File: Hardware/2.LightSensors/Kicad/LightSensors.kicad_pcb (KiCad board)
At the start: 2 copper layers, 0 parts

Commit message: Add update PCB dimension
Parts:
- added C1: 100nF, Capacitor_SMD:C_0402_1005Metric, F.Cu at (90.7, 86.9)
- added C2: 100nF, Capacitor_SMD:C_0402_1005Metric, F.Cu at (90.7, 88.8)
- added C3: 100nF, Capacitor_SMD:C_0402_1005Metric, F.Cu at (90.7, 90.8)
- added C4: 100nF, Capacitor_SMD:C_0402_1005Metric, F.Cu at (130.8, 110.5)
- added H1: MountingHole, MountingHole:MountingHole_3.2mm_M3_ISO7380, F.Cu at (81.3, 81.3)
- added H2: MountingHole, MountingHole:MountingHole_3.2mm_M3_ISO7380, F.Cu at (81.3, 121.9)
- added H3: MountingHole, MountingHole:MountingHole_3.2mm_M3_ISO7380, F.Cu at (172.7, 81.3)
- added H4: MountingHole, MountingHole:MountingHole_3.2mm_M3_ISO7380, F.Cu at (172.7, 122.2)
- added J1: Conn_01x10_Pin, Connector_JST:JST_PH_S10B-PH-K_1x10_P2.00mm_Horizontal, F.Cu at (147.6, 110.2)
- added JP1: SolderJumper_3_Open, Jumper:SolderJumper-3_P2.0mm_Open_TrianglePad1.0x1.5mm, F.Cu at (83.3, 102.1)
- added JP2: SolderJumper_3_Open, Jumper:SolderJumper-3_P2.0mm_Open_TrianglePad1.0x1.5mm, F.Cu at (86.4, 102.1)
- added JP3: SolderJumper_3_Open, Jumper:SolderJumper-3_P2.0mm_Open_TrianglePad1.0x1.5mm, F.Cu at (135.8, 113.1)
- added R1: 0, NetTie:NetTie-2_THT_Pad0.3mm, F.Cu at (84.1, 89.8)
- added R2: 0, NetTie:NetTie-2_THT_Pad0.3mm, F.Cu at (84.1, 91.4)
- added R3: 3.3M, Capacitor_SMD:C_0402_1005Metric, F.Cu at (90.7, 94.7)
- added R4: 10K, Resistor_SMD:R_0402_1005Metric, F.Cu at (143.3, 91.7)
- added R5: 10k, Resistor_SMD:R_0402_1005Metric, F.Cu at (143.3, 96.3)
- added R6: 10K, Capacitor_SMD:C_0402_1005Metric, F.Cu at (130.8, 114.4)
- added U1: AS7331, AS7331:OLGA-16, F.Cu at (104.6, 102.4)
- added U2: OPT3004, OPT3004:SON65P200X200X65-7N, F.Cu at (134.9, 121.8)
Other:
- board outline added: 101.6 x 50.8 mm

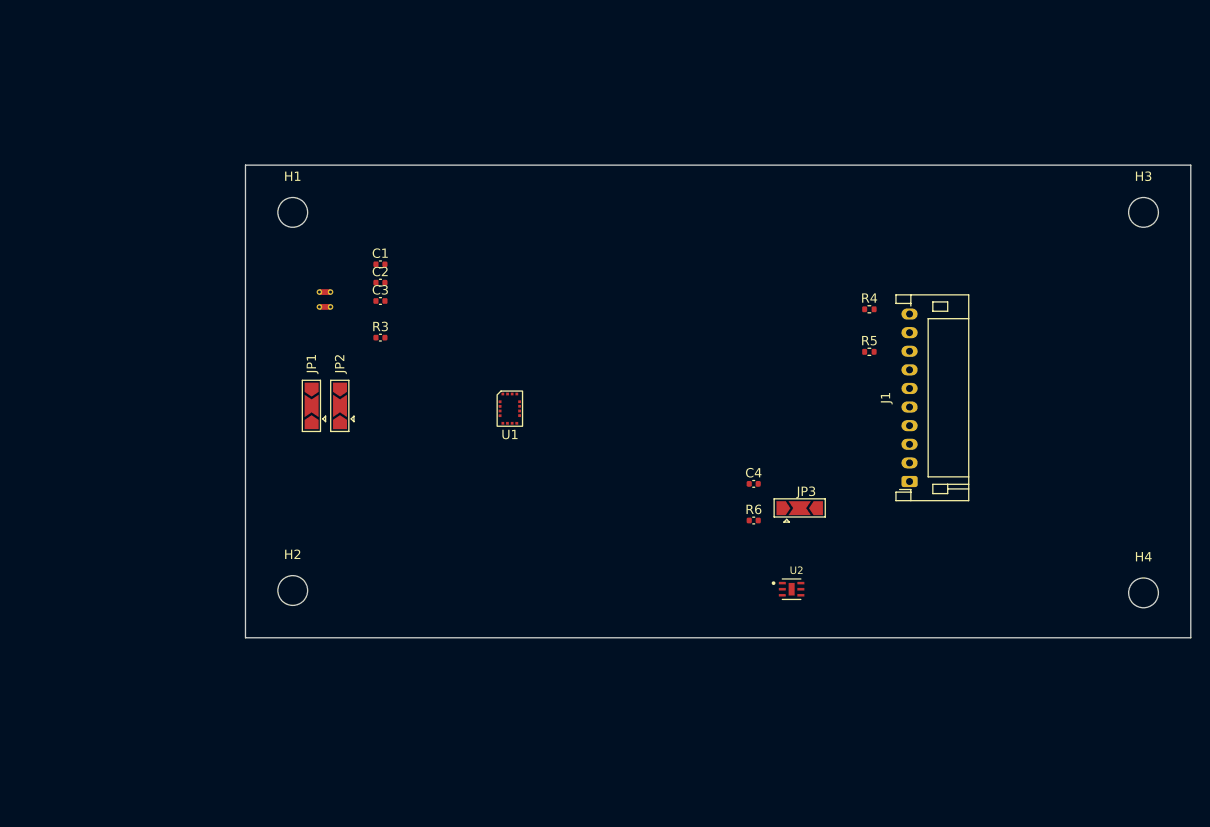
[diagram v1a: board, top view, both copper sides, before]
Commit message: Update PCB for LightSensors
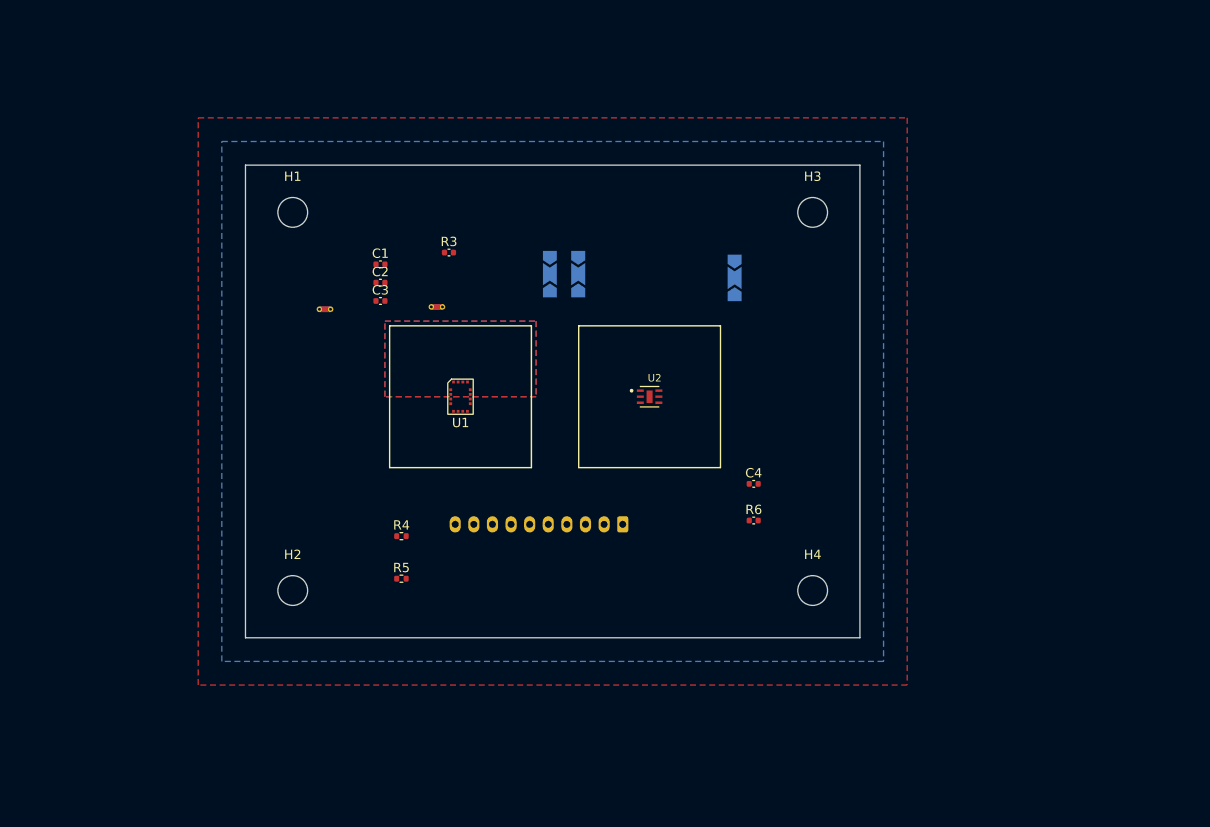
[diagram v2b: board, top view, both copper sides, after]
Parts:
- J1, JP1, JP2, JP3, R1, R2: moved to B.Cu
- moved R4 55.9 mm to (93.0, 116.1)
- moved R5 55.9 mm to (93.0, 120.7)
- moved H4 35.6 mm to (137.2, 121.9)
- moved H3 35.6 mm to (137.2, 81.3)
- moved JP1 32.0 mm to (112.0, 87.9)
- moved J1 31.2 mm to (116.7, 114.8), turned to 180 degrees
- moved JP2 26.6 mm to (108.9, 87.9)
- moved JP3 25.7 mm to (128.8, 88.3), turned to 90 degrees
- moved U2 25.7 mm to (119.6, 101.1)
- moved R2 13.2 mm to (97.4, 91.4), turned to 180 degrees
- moved R3 11.7 mm to (98.1, 85.6)
- moved U1 5.46 mm to (99.3, 101.1)
- moved R1 1.85 mm to (84.1, 91.7)
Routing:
- added copper zone on B.Cu, net +3.3V
- added copper zone on B.Cu, net +3.3VA
- added copper zone on F.Cu, net GND
- added copper zone on F.Cu, net GNDA
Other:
- board size 101.6 x 50.8 mm -> 66 x 50.8 mm

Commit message: Design initial version of PCB for light sensors
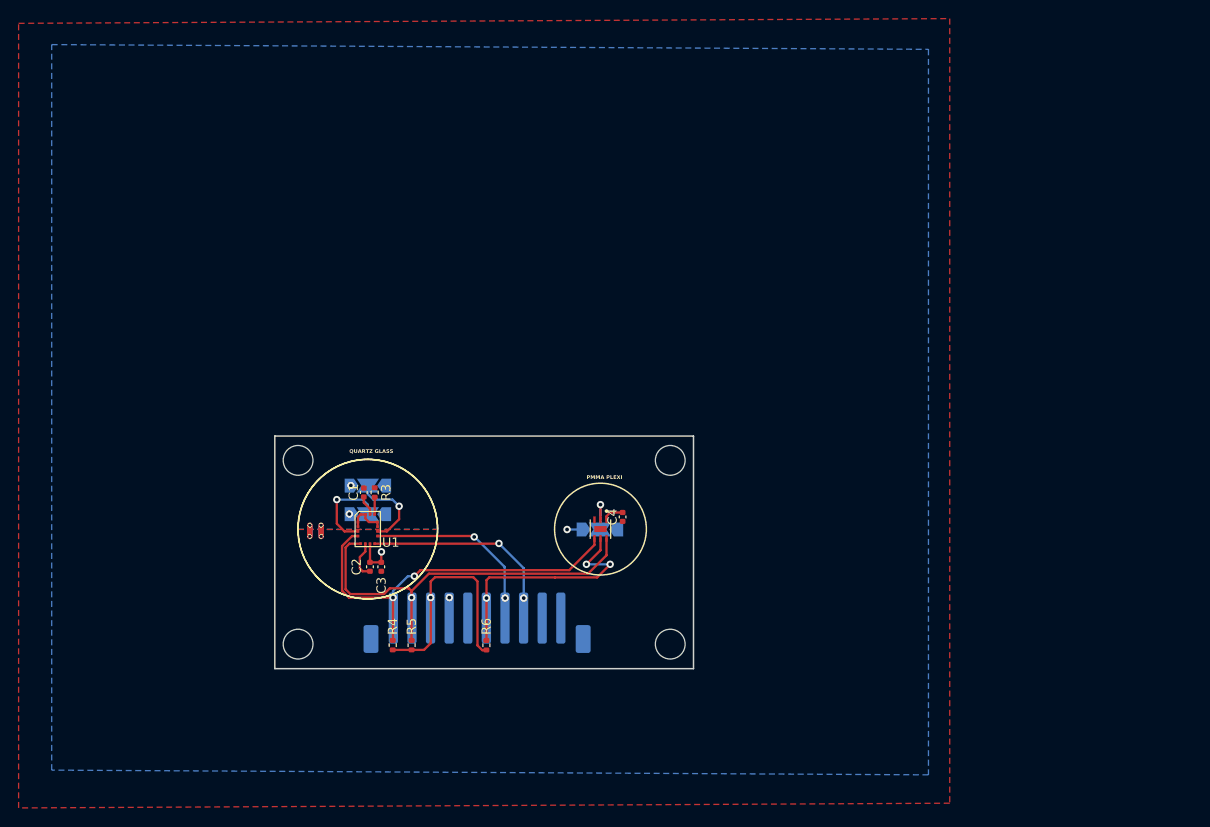
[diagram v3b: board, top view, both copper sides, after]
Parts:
- H1, H2, H3, H4: footprint MountingHole:MountingHole_3.2mm_M3_ISO7380 -> MountingHole:MountingHole_3.2mm_M3
- J1: footprint Connector_JST:JST_PH_S10B-PH-K_1x10_P2.00mm_Horizontal -> Connector_JST:JST_PH_B10B-PH-SM4-TB_1x10-1MP_P2.00mm_Vertical
- R2: moved to F.Cu
- R3, R6: footprint Capacitor_SMD:C_0402_1005Metric -> Resistor_SMD:R_0402_1005Metric
- moved H4 55.6 mm to (81.9, 127.7)
- moved H3 48.9 mm to (121.9, 127.7)
- moved H2 42.9 mm to (121.9, 107.9)
- moved A0 34.3 mm to (89.4, 113.7), turned to 0 degrees
- moved R6 31.7 mm to (102.1, 127.8), turned to 90 degrees
- moved ADDR 30.7 mm to (114.3, 115.4), turned to 0 degrees
- moved C2 30.6 mm to (89.6, 119.4), turned to -90 degrees
- moved A1 30.0 mm to (89.4, 110.6), turned to 0 degrees
- moved C3 28.6 mm to (90.8, 119.4), turned to -90 degrees
- moved R2 28.5 mm to (83.1, 116.1), turned to 90 degrees
- moved R3 27.0 mm to (90.1, 111.4), turned to 90 degrees
- moved H1 26.7 mm to (81.9, 107.9)
- moved C1 24.6 mm to (88.9, 111.4), turned to 90 degrees
- moved R1 24.4 mm to (84.3, 116.1), turned to 90 degrees
- moved J1 18.9 mm to (101.1, 125.4), turned to 0 degrees
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- renumbered JP1 to A0, JP2 to A1, JP3 to ADDR
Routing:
- net I2C_SDA: track 0.00 -> 43.6 mm, vias 0 -> 1
- net I2C_SCL: track 0.00 -> 42.5 mm, vias 0 -> 2
- net +3.3V: track 0.00 -> 33.3 mm, vias 0 -> 2
- net OPT3004_INT: track 0.00 -> 26.5 mm, vias 0 -> 3
- net AS7331_READY: track 0.00 -> 22.5 mm, vias 0 -> 2
- net AS7331_SYN: track 0.00 -> 20.5 mm, vias 0 -> 2
- net ADDR0: track 0.00 -> 9.78 mm, vias 0 -> 1
- net ADDR1: track 0.00 -> 9.08 mm, vias 0 -> 1
- net GND: track 0.00 -> 5.65 mm, vias 0 -> 2
- net GNDA: track 0.00 -> 4.36 mm, vias 0 -> 2
- net Net-(JP3-C): track 0.00 -> 4.24 mm, vias 0 -> 1
- net +3.3VA: track 0.00 -> 2.15 mm
- net Net-(U1-REXT): track 0.00 -> 1.85 mm
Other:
- board size 66 x 50.8 mm -> 45 x 25 mm
- board text added: "1"
- board text added: "1 0"
- board text added: "Address |A1 |A0 0x74 |0 |0 0x75 |0 |1 0x76 |1 |0 0x77 |1 |1"
- board text added: "Address |ADDR 0x44 |0 0x45 |1"
- board text added: "PMMA PLEXI"
- board text added: "QUARTZ GLASS"

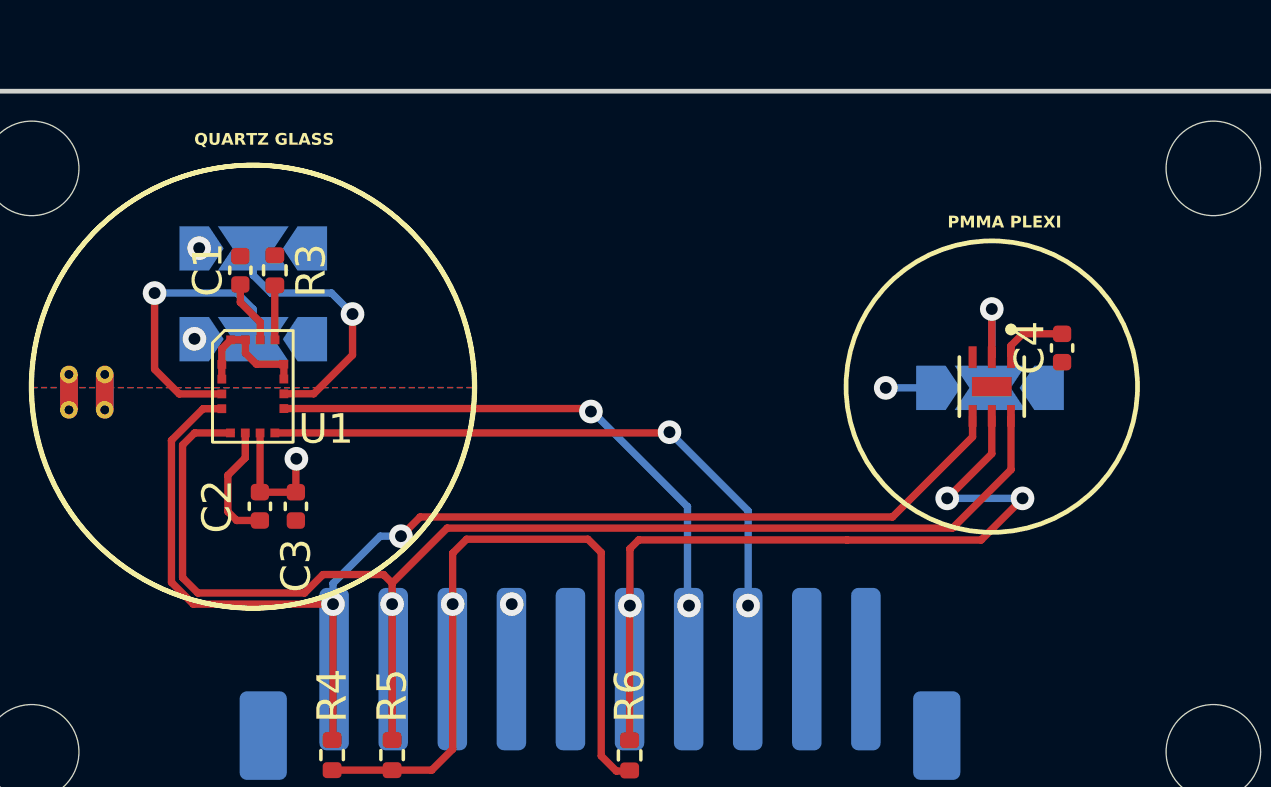
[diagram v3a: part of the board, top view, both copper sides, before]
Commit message: Add signal names on silkscreen and add connector 3dmodel
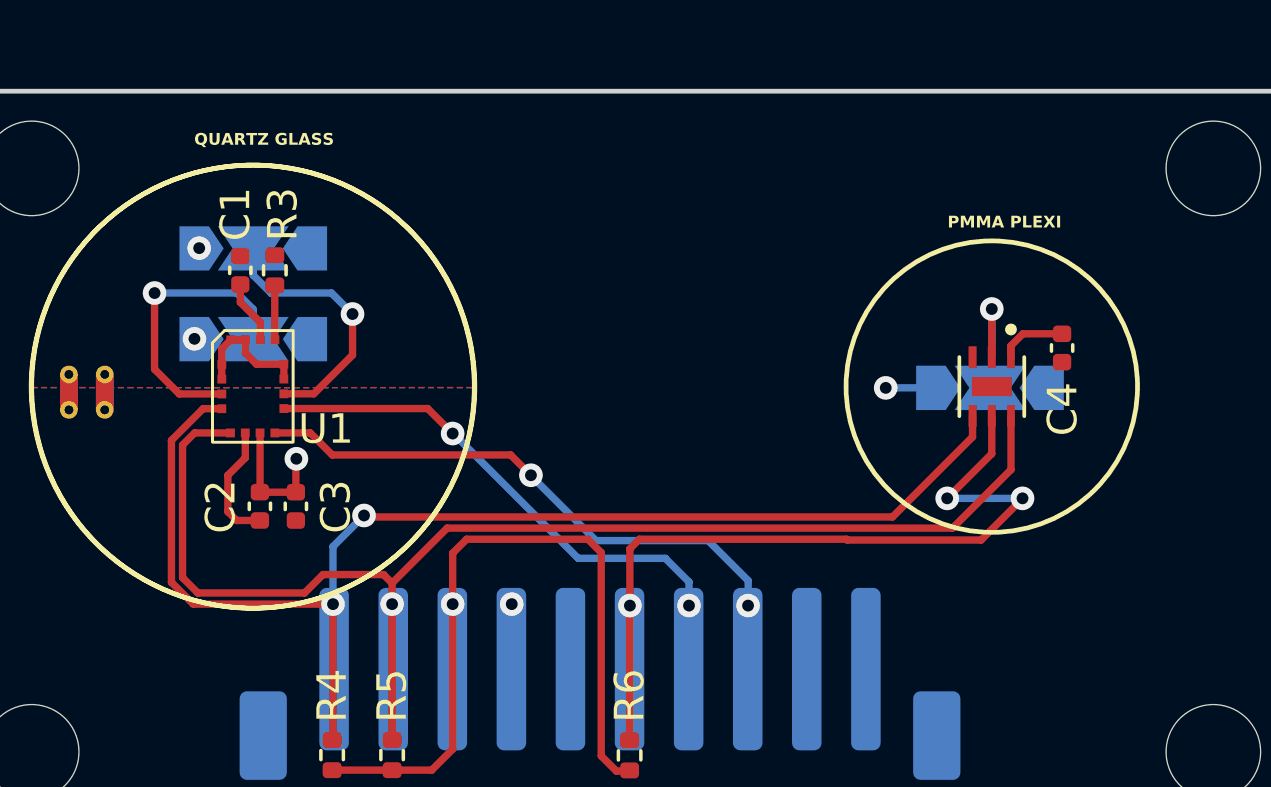
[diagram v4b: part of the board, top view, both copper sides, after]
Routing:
- net AS7331_SYN: track 20.5 -> 19.1 mm
- net AS7331_READY: track 22.5 -> 21.1 mm
- net I2C_SCL: track 42.5 -> 43.2 mm
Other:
- board text added: "3V3"
- board text added: "AS7331_READY"
- board text added: "AS7331_SYN"
- board text added: "GND"
- board text added: "I2C_SCL"
- board text added: "OPT3004_INT"
- board text added: "SCL"
- board text added: "SDA"

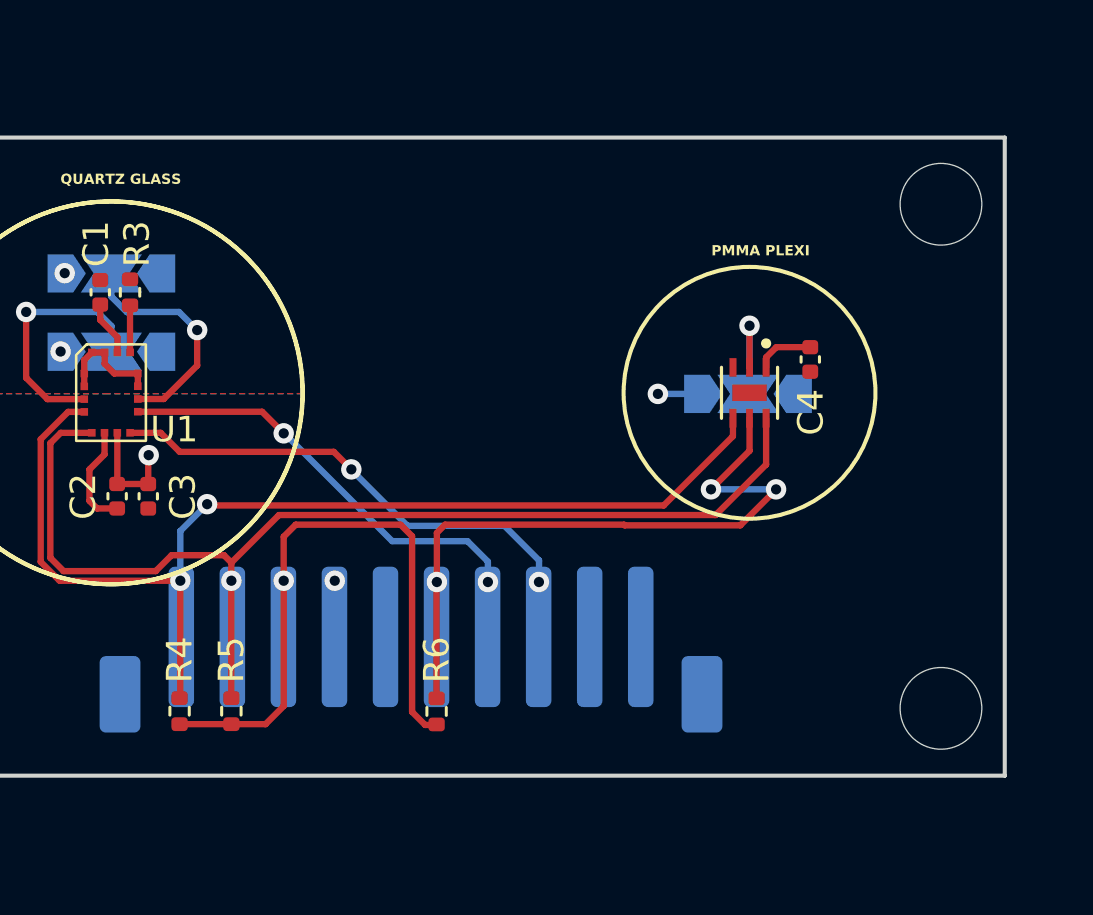
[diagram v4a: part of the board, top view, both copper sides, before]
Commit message: Update pcb due to connector pinout fix
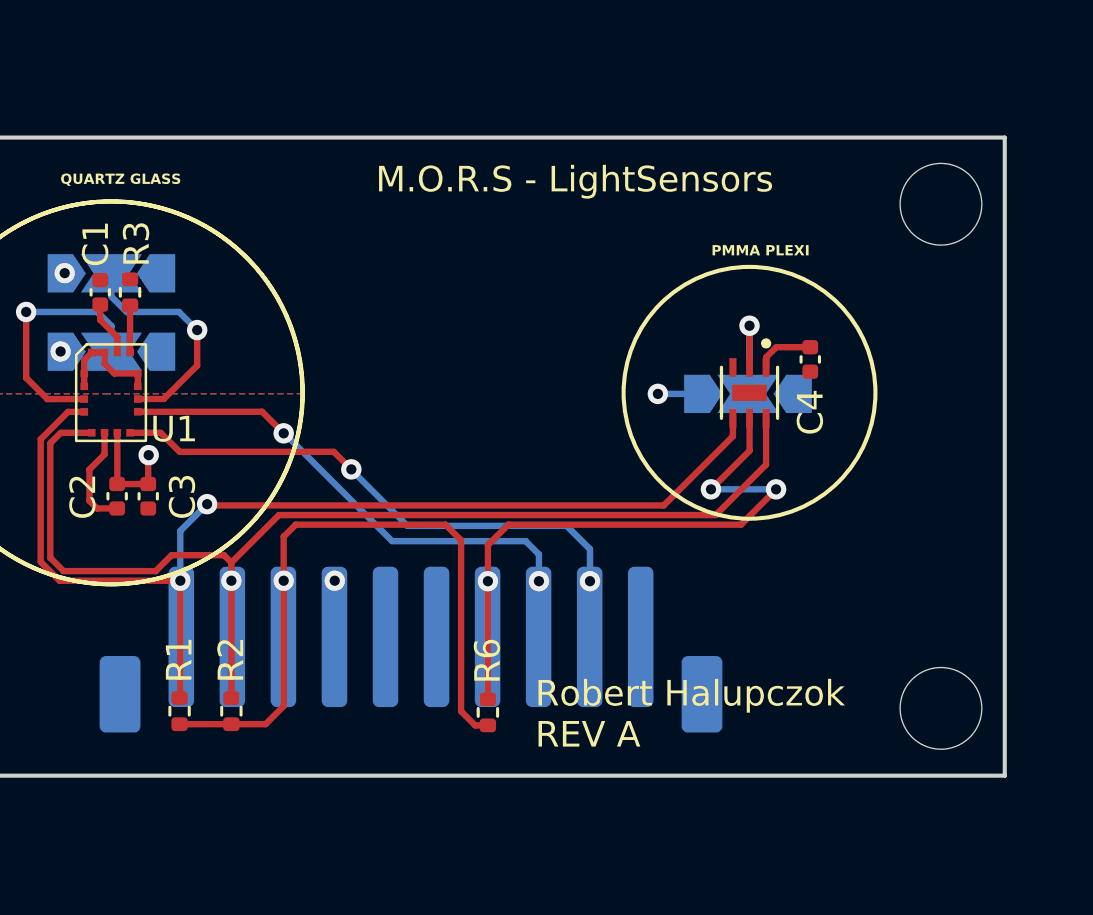
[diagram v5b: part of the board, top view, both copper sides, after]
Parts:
- moved R6 2.01 mm to (104.1, 127.8)
- renumbered A0 to A2, ADDR to ADDR1, R4 to R1, R5 to R2, R2 to R4, R1 to R5
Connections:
- J1 pad 6: OPT3004_INT -> unconnected-(J1-Pin_6-Pad6)
- J1 pad 7: AS7331_SYN -> OPT3004_INT
- J1 pad 8: AS7331_READY -> AS7331_SYN
- J1 pad 9: unconnected-(J1-Pin_9-Pad9) -> AS7331_READY
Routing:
- net AS7331_SYN: track 19.1 -> 21.3 mm
- net +3.3V: track 33.3 -> 35.2 mm
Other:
- board text added: "M.O.R.S - LightSensors"
- board text added: "Robert Halupczok REV A"
- board text removed: "I2C_SCL"
